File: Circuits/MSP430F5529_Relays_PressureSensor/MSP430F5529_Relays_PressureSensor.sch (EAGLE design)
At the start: 15 parts, among them IC1 UA78M05DCY, J2 OSTTG0451XBNO_THP, K1 AQV21SMD, K2 AQV21SMD, U2 SSCMRNN015PA3A3

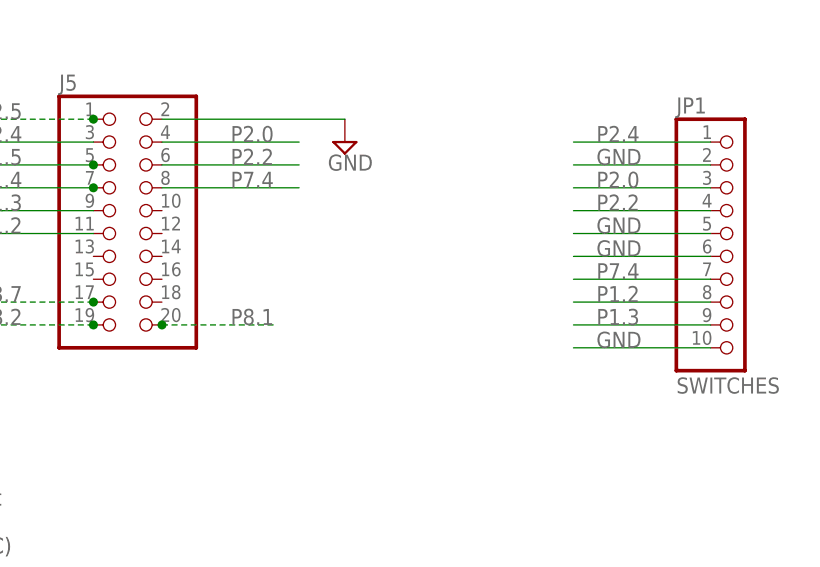
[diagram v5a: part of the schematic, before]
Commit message: Replace P7.4 with P2.3 as P7.4 is not IRQ-capable
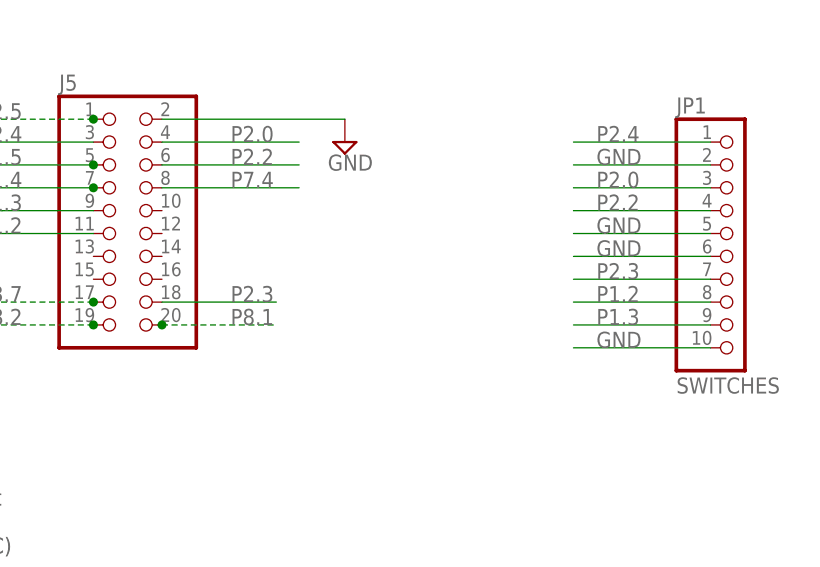
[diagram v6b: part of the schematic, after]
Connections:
- new net P2.3: J5.18, JP1.7
- net P7.4: no longer JP1.7
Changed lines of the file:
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@@
 <grid distance="0.1" unitdist="inch" unit="inch" style="lines" multiple="1" display="no" altdistance="0.01" altunitdist="inch" altunit="inch"/>
 <layers>
-<layer number="1" name="Top" color="4" fill="1" visible="yes" active="no"/>
-<layer number="2" name="Route2" color="16" fill="1" visible="yes" active="no"/>
-<layer number="3" name="Route3" color="17" fill="1" visible="yes" active="no"/>
-<layer number="4" name="Route4" color="18" fill="1" visible="yes" active="no"/>
-<layer number="5" name="Route5" color="19" fill="1" visible="yes" active="no"/>
-<layer number="6" name="Route6" color="25" fill="1" visible="yes" active="no"/>
-<layer number="7" name="Route7" color="26" fill="1" visible="yes" active="no"/>
-<layer number="8" name="Route8" color="27" fill="1" visible="yes" active="no"/>
-<layer number="9" name="Route9" color="28" fill="1" visible="yes" active="no"/>
-<layer number="10" name="Route10" color="29" fill="1" visible="yes" active="no"/>
-<layer number="11" name="Route11" color="30" fill="1" visible="yes" active="no"/>
-<layer number="12" name="Route12" color="20" fill="1" visible="yes" active="no"/>
-<layer number="13" name="Route13" color="21" fill="1" visible="yes" active="no"/>
-<layer number="14" name="Route14" color="22" fill="1" visible="yes" active="no"/>
-<layer number="15" name="Route15" color="23" fill="1" visible="yes" active="no"/>
-<layer number="16" name="Bottom" color="1" fill="1" visible="yes" active="no"/>
-<layer number="17" name="Pads" color="2" fill="1" visible="yes" active="no"/>
-<layer number="18" name="Vias" color="2" fill="1" visible="yes" active="no"/>
-<layer number="19" name="Unrouted" color="6" fill="1" visible="yes" active="no"/>
-<layer number="20" name="Dimension" color="24" fill="1" visible="yes" active="no"/>
-<layer number="21" name="tPlace" color="7" fill="1" visible="yes" active="no"/>
-<layer number="22" name="bPlace" color="7" fill="1" visible="yes" active="no"/>
-<layer number="23" name="tOrigins" color="15" fill="1" visible="yes" active="no"/>
-<layer number="24" name="bOrigins" color="15" fill="1" visible="yes" active="no"/>
-<layer number="25" name="tNames" color="7" fill="1" visible="yes" active="no"/>
-<layer number="26" name="bNames" color="7" fill="1" visible="yes" active="no"/>
-<layer number="27" name="tValues" color="7" fill="1" visible="yes" active="no"/>
-<layer number="28" name="bValues" color="7" fill="1" visible="yes" active="no"/>
+<layer number="1" name="Top" color="4" fill="1" visible="no" active="no"/>
+<layer number="2" name="Route2" color="16" fill="1" visible="no" active="no"/>
+<layer number="3" name="Route3" color="17" fill="1" visible="no" active="no"/>
+<layer number="4" name="Route4" color="18" fill="1" visible="no" active="no"/>
+<layer number="5" name="Route5" color="19" fill="1" visible="no" active="no"/>
+<layer number="6" name="Route6" color="25" fill="1" visible="no" active="no"/>
+<layer number="7" name="Route7" color="26" fill="1" visible="no" active="no"/>
+<layer number="8" name="Route8" color="27" fill="1" visible="no" active="no"/>
+<layer number="9" name="Route9" color="28" fill="1" visible="no" active="no"/>
+<layer number="10" name="Route10" color="29" fill="1" visible="no" active="no"/>
+<layer number="11" name="Route11" color="30" fill="1" visible="no" active="no"/>
+<layer number="12" name="Route12" color="20" fill="1" visible="no" active="no"/>
+<layer number="13" name="Route13" color="21" fill="1" visible="no" active="no"/>
+<layer number="14" name="Route14" color="22" fill="1" visible="no" active="no"/>
+<layer number="15" name="Route15" color="23" fill="1" visible="no" active="no"/>
+<layer number="16" name="Bottom" color="1" fill="1" visible="no" active="no"/>
+<layer number="17" name="Pads" color="2" fill="1" visible="no" active="no"/>
+<layer number="18" name="Vias" color="2" fill="1" visible="no" active="no"/>
+<layer number="19" name="Unrouted" color="6" fill="1" visible="no" active="no"/>
+<layer number="20" name="Dimension" color="24" fill="1" visible="no" active="no"/>
+<layer number="21" name="tPlace" color="7" fill="1" visible="no" active="no"/>
+<layer number="22" name="bPlace" color="7" fill="1" visible="no" active="no"/>
+<layer number="23" name="tOrigins" color="15" fill="1" visible="no" active="no"/>
+<layer number="24" name="bOrigins" color="15" fill="1" visible="no" active="no"/>
+<layer number="25" name="tNames" color="7" fill="1" visible="no" active="no"/>
+<layer number="26" name="bNames" color="7" fill="1" visible="no" active="no"/>
+<layer number="27" name="tValues" color="7" fill="1" visible="no" active="no"/>
+<layer number="28" name="bValues" color="7" fill="1" visible="no" active="no"/>
 <layer number="29" name="tStop" color="7" fill="3" visible="no" active="no"/>
 <layer number="30" name="bStop" color="7" fill="6" visible="no" active="no"/>
@@
 <layer number="35" name="tGlue" color="7" fill="4" visible="no" active="no"/>
 <layer number="36" name="bGlue" color="7" fill="5" visible="no" active="no"/>
-<layer number="37" name="tTest" color="7" fill="1" visible="yes" active="no"/>
-<layer number="38" name="bTest" color="7" fill="1" visible="yes" active="no"/>
+<layer number="37" name="tTest" color="7" fill="1" visible="no" active="no"/>
+<layer number="38" name="bTest" color="7" fill="1" visible="no" active="no"/>
 <layer number="39" name="tKeepout" color="4" fill="11" visible="no" active="no"/>
 <layer number="40" name="bKeepout" color="1" fill="11" visible="no" active="no"/>
@@
 <layer number="44" name="Drills" color="7" fill="1" visible="no" active="no"/>
 <layer number="45" name="Holes" color="7" fill="1" visible="no" active="no"/>
-<layer number="46" name="Milling" color="3" fill="1" visible="yes" active="no"/>
-<layer number="47" name="Measures" color="7" fill="1" visible="yes" active="no"/>
-<layer number="48" name="Document" color="7" fill="1" visible="yes" active="no"/>
-<layer number="49" name="Reference" color="7" fill="1" visible="yes" active="no"/>
-<layer number="50" name="dxf" color="7" fill="1" visible="yes" active="no"/>
-<layer number="51" name="tDocu" color="7" fill="1" visible="yes" active="no"/>
-<layer number="52" name="bDocu" color="7" fill="1" visible="yes" active="no"/>
-<layer number="53" name="tGND_GNDA" color="7" fill="9" visible="yes" active="no"/>
-<layer number="54" name="bGND_GNDA" color="1" fill="9" visible="yes" active="no"/>
+<layer number="46" name="Milling" color="3" fill="1" visible="no" active="no"/>
+<layer number="47" name="Measures" color="7" fill="1" visible="no" active="no"/>
+<layer number="48" name="Document" color="7" fill="1" visible="no" active="no"/>
+<layer number="49" name="Reference" color="7" fill="1" visible="no" active="no"/>
+<layer number="50" name="dxf" color="7" fill="1" visible="no" active="no"/>
+<layer number="51" name="tDocu" color="7" fill="1" visible="no" active="no"/>
+<layer number="52" name="bDocu" color="7" fill="1" visible="no" active="no"/>
+<layer number="53" name="tGND_GNDA" color="7" fill="9" visible="no" active="no"/>
+<layer number="54" name="bGND_GNDA" color="1" fill="9" visible="no" active="no"/>
 <layer number="88" name="SimResults" color="9" fill="1" visible="yes" active="yes"/>
 <layer number="89" name="SimProbes" color="9" fill="1" visible="yes" active="yes"/>
@@
 <label x="101.6" y="17.78" size="1.778" layer="95"/>
 </segment>
-<segment>
-<pinref part="JP1" gate="A" pin="7"/>
-<wire x1="154.94" y1="7.62" x2="139.7" y2="7.62" width="0.1524" layer="91"/>
-<label x="142.24" y="7.62" size="1.778" layer="95"/>
-</segment>
 </net>
 <net name="P1.2" class="0">
@@
 </segment>
 </net>
+<net name="P2.3" class="0">
+<segment>
+<pinref part="J5" gate="A" pin="18"/>
+<wire x1="93.98" y1="5.08" x2="106.68" y2="5.08" width="0.1524" layer="91"/>
+<label x="101.6" y="5.08" size="1.778" layer="95"/>
+</segment>
+<segment>
+<pinref part="JP1" gate="A" pin="7"/>
+<wire x1="154.94" y1="7.62" x2="139.7" y2="7.62" width="0.1524" layer="91"/>
+<label x="142.24" y="7.62" size="1.778" layer="95"/>
+</segment>
+</net>
